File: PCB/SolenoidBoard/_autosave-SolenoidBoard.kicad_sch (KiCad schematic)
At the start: 38 parts, among them IC1 NJW4132U2-B-TE2, J1 XT30, J2 Con_45V, J3 Con_45V, J4 Conn_01x02, J5 Con_GND, J6 Con_GND, J7 Conn_01x02, J8 Conn_01x06_Pin, J9 Conn_01x02, Q1 Q_PMOS_GSD, Q3 TPH11006NL,LQ_S, Q4 TPH11006NL,LQ_S, Q5 TPH11006NL,LQ_S, U1 TLP293, U2 TLP293, U3 TLP293, U4 TLP293

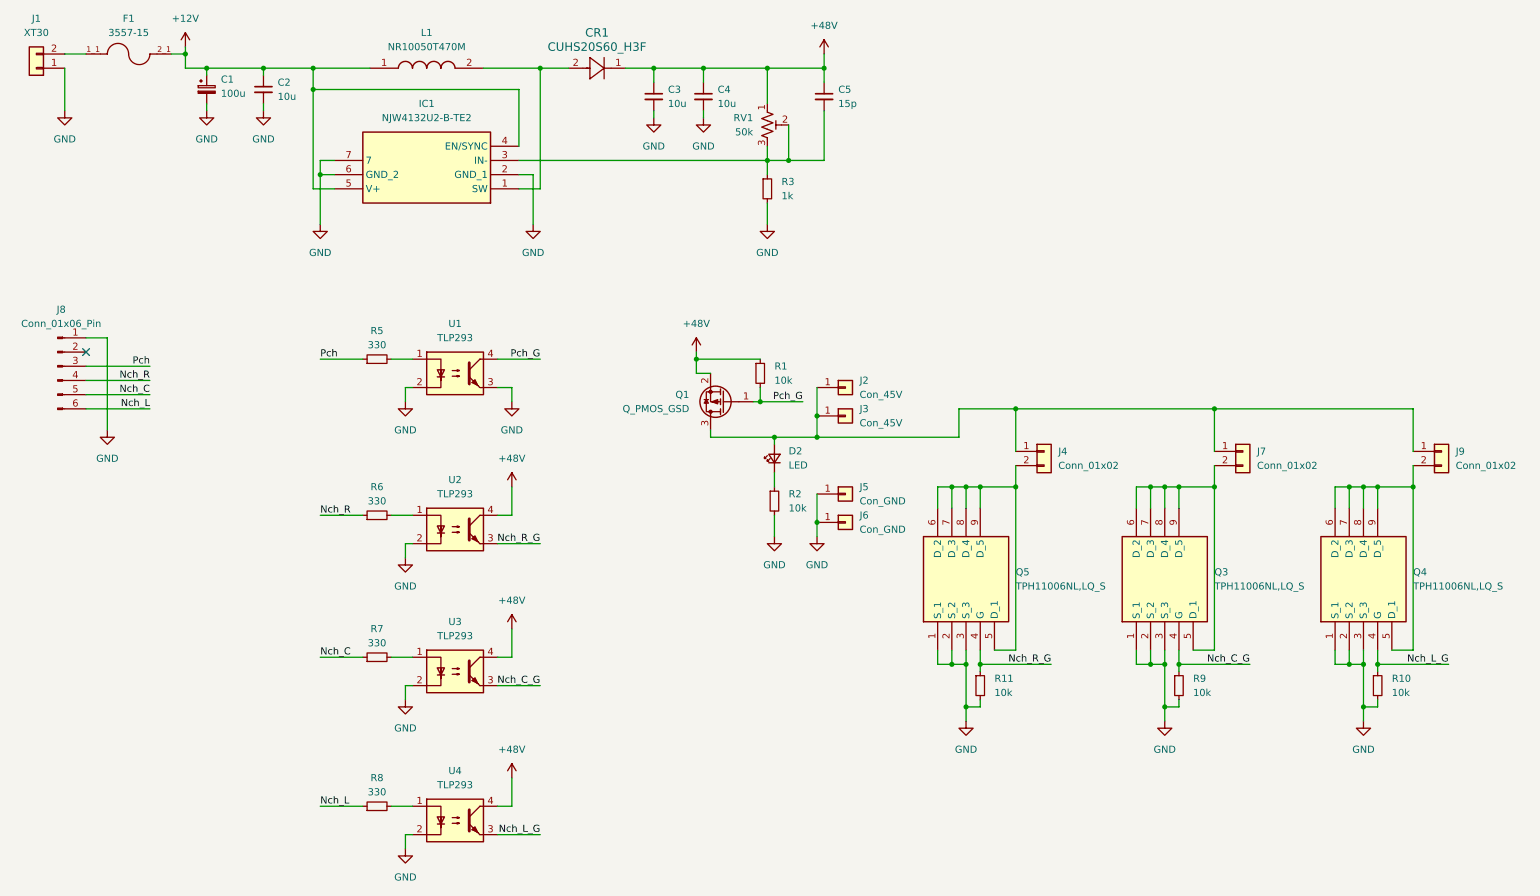
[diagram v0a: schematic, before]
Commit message: 部品配置終わり
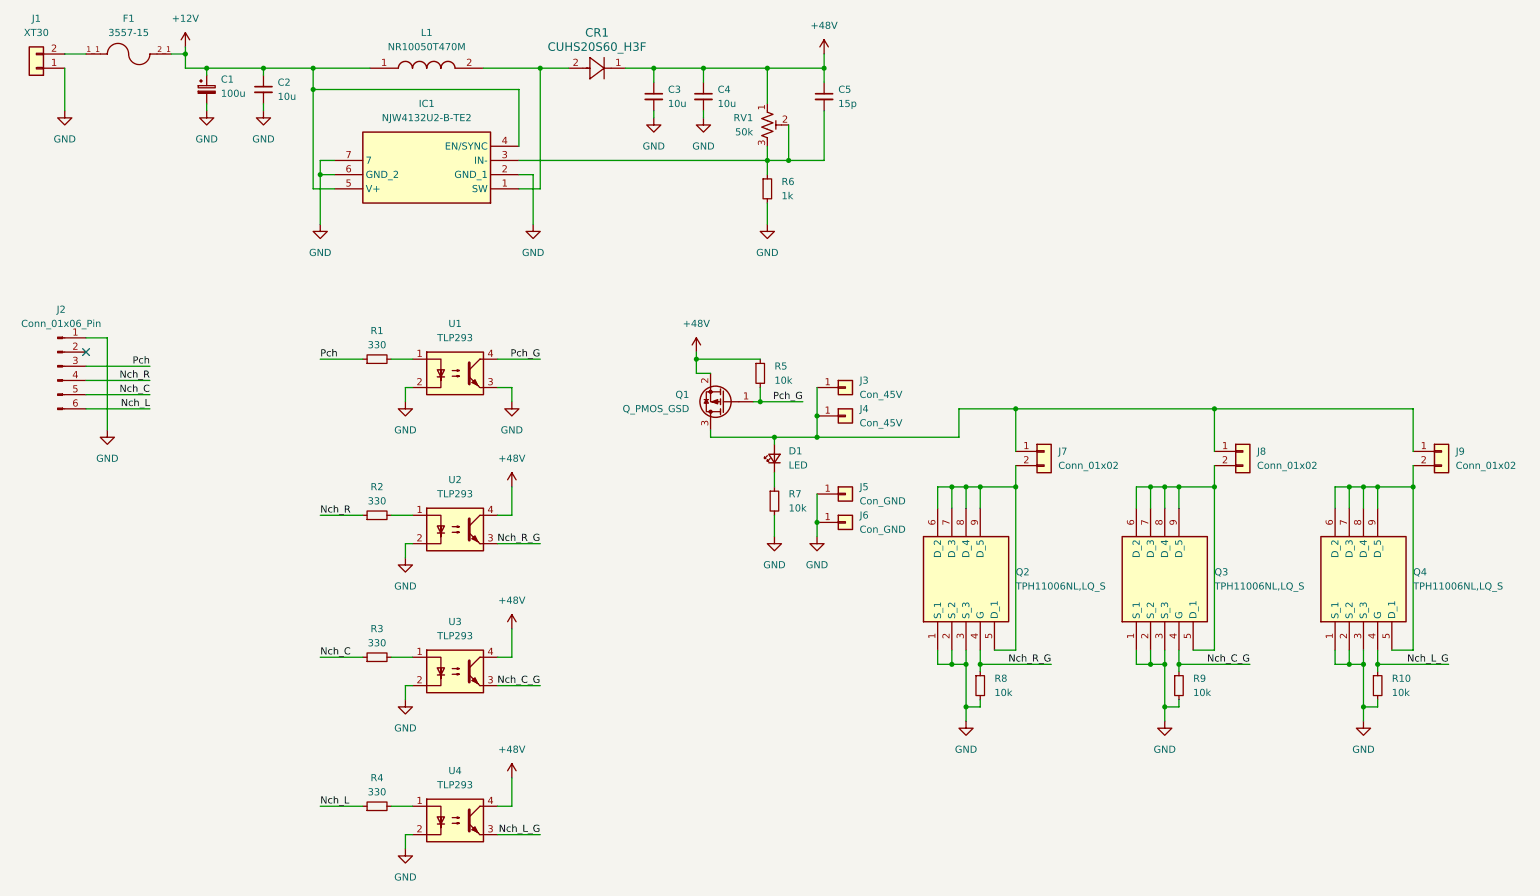
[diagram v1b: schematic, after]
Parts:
- CR1: footprint SOD-323HEUS2H_TOS -> CUHS20S60:SOD-323HEUS2H_TOS
- renumbered D2 to D1, J8 to J2, J2 to J3, J3 to J4, J4 to J7, J7 to J8, Q5 to Q2, R5 to R1, R6 to R2, R7 to R3, R8 to R4, R1 to R5, R3 to R6, R2 to R7, R11 to R8
